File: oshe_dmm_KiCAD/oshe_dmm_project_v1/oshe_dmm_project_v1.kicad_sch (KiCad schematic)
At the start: 65 parts, among them J1 FTDI Basic, J2 USB_C_Receptacle_PowerOnly_6P, J3 ON/OFF, J4 Conn_01x16, SW1 SW_Push, SW2 SW_Rotary_1x4_MP, U1 ATmega328P-A, U2 INA219BxD, U3 BQ24075RGT, U4 LM317_SOT-223, U5 ADS1115IDGS, Y1 16MHz

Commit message: made some more changes!
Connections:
- net GND: now also RV2.3; no longer RV2.2
- net at J4.3 (Pin_3): now also RV2.2; no longer RV2.3
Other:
- moved on the sheet: RV2
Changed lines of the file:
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@@
 	(wire
 		(pts
+			(xy 166.37 45.72) (xy 172.72 45.72)
+		)
+		(stroke
+			(width 0)
+			(type default)
+		)
+	)
+	(wire
+		(pts
 			(xy 332.74 41.91) (xy 345.44 41.91)
 		)
@@
 	(wire
 		(pts
-			(xy 152.4 73.66) (xy 200.66 73.66)
+			(xy 152.4 72.39) (xy 200.66 72.39)
+		)
+		(stroke
+			(width 0)
+			(type default)
+		)
+	)
+	(wire
+		(pts
+			(xy 152.4 49.53) (xy 162.56 49.53)
 		)
 		(stroke
@@
 	(wire
 		(pts
-			(xy 205.74 78.74) (xy 205.74 30.48)
+			(xy 205.74 77.47) (xy 205.74 30.48)
 		)
 		(stroke
@@
 	(wire
 		(pts
-			(xy 152.4 44.45) (xy 158.75 44.45)
-		)
-		(stroke
-			(width 0)
-			(type default)
-		)
-	)
-	(wire
-		(pts
 			(xy 243.84 111.76) (xy 254 111.76)
 		)
@@
 	(wire
 		(pts
-			(xy 193.04 66.04) (xy 193.04 30.48)
+			(xy 193.04 64.77) (xy 193.04 30.48)
 		)
 		(stroke
@@
 	(wire
 		(pts
-			(xy 152.4 60.96) (xy 180.34 60.96)
+			(xy 152.4 59.69) (xy 180.34 59.69)
 		)
 		(stroke
@@
 	(wire
 		(pts
-			(xy 175.26 55.88) (xy 175.26 30.48)
+			(xy 175.26 54.61) (xy 175.26 30.48)
 		)
 		(stroke
@@
 	(wire
 		(pts
-			(xy 152.4 71.12) (xy 198.12 71.12)
+			(xy 152.4 69.85) (xy 198.12 69.85)
 		)
 		(stroke
@@
 	(wire
 		(pts
-			(xy 152.4 58.42) (xy 177.8 58.42)
+			(xy 152.4 57.15) (xy 177.8 57.15)
 		)
 		(stroke
@@
 	(wire
 		(pts
-			(xy 152.4 49.53) (xy 162.56 49.53)
-		)
-		(stroke
-			(width 0)
-			(type default)
-		)
-	)
-	(wire
-		(pts
 			(xy 233.68 58.42) (xy 233.68 60.96)
 		)
@@
 	(wire
 		(pts
-			(xy 195.58 68.58) (xy 195.58 30.48)
+			(xy 195.58 67.31) (xy 195.58 30.48)
 		)
 		(stroke
@@
 	(wire
 		(pts
-			(xy 180.34 60.96) (xy 180.34 30.48)
+			(xy 180.34 59.69) (xy 180.34 30.48)
 		)
 		(stroke
@@
 	(wire
 		(pts
-			(xy 152.4 66.04) (xy 193.04 66.04)
+			(xy 152.4 64.77) (xy 193.04 64.77)
 		)
 		(stroke
@@
 	(wire
 		(pts
+			(xy 172.72 45.72) (xy 172.72 30.48)
+		)
+		(stroke
+			(width 0)
+			(type default)
+		)
+	)
+	(wire
+		(pts
 			(xy 66.04 142.24) (xy 66.04 146.05)
 		)
@@
 	(wire
 		(pts
-			(xy 152.4 55.88) (xy 175.26 55.88)
+			(xy 152.4 54.61) (xy 175.26 54.61)
 		)
 		(stroke
@@
 	(wire
 		(pts
+			(xy 152.4 41.91) (xy 162.56 41.91)
+		)
+		(stroke
+			(width 0)
+			(type default)
+		)
+	)
+	(wire
+		(pts
 			(xy 76.2 161.29) (xy 80.01 161.29)
 		)
@@
 	(wire
 		(pts
-			(xy 152.4 78.74) (xy 205.74 78.74)
+			(xy 152.4 77.47) (xy 205.74 77.47)
 		)
 		(stroke
@@
 	(wire
 		(pts
-			(xy 172.72 44.45) (xy 172.72 30.48)
-		)
-		(stroke
-			(width 0)
-			(type default)
-		)
-	)
-	(wire
-		(pts
 			(xy 261.62 33.02) (xy 285.75 33.02)
 		)
@@
 	(wire
 		(pts
-			(xy 203.2 76.2) (xy 152.4 76.2)
+			(xy 203.2 74.93) (xy 152.4 74.93)
 		)
 		(stroke
@@
 	(wire
 		(pts
-			(xy 152.4 68.58) (xy 195.58 68.58)
+			(xy 152.4 67.31) (xy 195.58 67.31)
 		)
 		(stroke
@@
 	(wire
 		(pts
-			(xy 200.66 73.66) (xy 200.66 30.48)
+			(xy 200.66 72.39) (xy 200.66 30.48)
 		)
 		(stroke
@@
 	(wire
 		(pts
-			(xy 166.37 44.45) (xy 172.72 44.45)
-		)
-		(stroke
-			(width 0)
-			(type default)
-		)
-	)
-	(wire
-		(pts
 			(xy 332.74 49.53) (xy 336.55 49.53)
 		)
@@
 	(wire
 		(pts
-			(xy 177.8 58.42) (xy 177.8 30.48)
+			(xy 177.8 57.15) (xy 177.8 30.48)
 		)
 		(stroke
@@
 	(wire
 		(pts
-			(xy 198.12 71.12) (xy 198.12 30.48)
+			(xy 198.12 69.85) (xy 198.12 30.48)
 		)
 		(stroke
@@
 	(wire
 		(pts
-			(xy 203.2 30.48) (xy 203.2 76.2)
+			(xy 203.2 30.48) (xy 203.2 74.93)
 		)
 		(stroke
@@
 	(wire
 		(pts
-			(xy 162.56 49.53) (xy 162.56 48.26)
-		)
-		(stroke
-			(width 0)
-			(type default)
-		)
-	)
-	(wire
-		(pts
 			(xy 228.6 157.48) (xy 198.12 157.48)
 		)
@@
 	(global_label "GND"
 		(shape input)
-		(at 152.4 78.74 180)
+		(at 152.4 77.47 180)
 		(fields_autoplaced yes)
 		(effects
@@
 		)
 		(property "Intersheetrefs" "${INTERSHEET_REFS}"
-			(at 145.5443 78.74 0)
+			(at 145.5443 77.47 0)
 			(effects
 				(font
@@
 	(global_label "D5"
 		(shape input)
-		(at 152.4 66.04 180)
+		(at 152.4 64.77 180)
 		(fields_autoplaced yes)
 		(effects
@@
 		)
 		(property "Intersheetrefs" "${INTERSHEET_REFS}"
-			(at 146.9353 66.04 0)
+			(at 146.9353 64.77 0)
 			(effects
 				(font
@@
 	(global_label "GND"
 		(shape input)
-		(at 152.4 58.42 180)
+		(at 152.4 57.15 180)
 		(fields_autoplaced yes)
 		(effects
@@
 		)
 		(property "Intersheetrefs" "${INTERSHEET_REFS}"
-			(at 145.5443 58.42 0)
+			(at 145.5443 57.15 0)
 			(effects
 				(font
@@
 	(global_label "+5V"
 		(shape input)
-		(at 152.4 76.2 180)
+		(at 152.4 74.93 180)
 		(fields_autoplaced yes)
 		(effects
@@
 		)
 		(property "Intersheetrefs" "${INTERSHEET_REFS}"
-			(at 145.5443 76.2 0)
+			(at 145.5443 74.93 0)
 			(effects
 				(font
@@
 	(global_label "MISO{slash}D12"
 		(shape input)
-		(at 152.4 60.96 180)
+		(at 152.4 59.69 180)
 		(fields_autoplaced yes)
 		(effects
@@
 		)
 		(property "Intersheetrefs" "${INTERSHEET_REFS}"
-			(at 139.7991 60.96 0)
+			(at 139.7991 59.69 0)
 			(effects
 				(font
@@
 	(global_label "D4"
 		(shape input)
-		(at 152.4 68.58 180)
+		(at 152.4 67.31 180)
 		(fields_autoplaced yes)
 		(effects
@@
 		)
 		(property "Intersheetrefs" "${INTERSHEET_REFS}"
-			(at 146.9353 68.58 0)
+			(at 146.9353 67.31 0)
 			(effects
 				(font
@@
 	(global_label "D3"
 		(shape input)
-		(at 152.4 71.12 180)
+		(at 152.4 69.85 180)
 		(fields_autoplaced yes)
 		(effects
@@
 		)
 		(property "Intersheetrefs" "${INTERSHEET_REFS}"
-			(at 146.9353 71.12 0)
+			(at 146.9353 69.85 0)
 			(effects
 				(font
@@
 	(global_label "D2"
 		(shape input)
-		(at 152.4 73.66 180)
+		(at 152.4 72.39 180)
 		(fields_autoplaced yes)
 		(effects
@@
 		)
 		(property "Intersheetrefs" "${INTERSHEET_REFS}"
-			(at 146.9353 73.66 0)
+			(at 146.9353 72.39 0)
 			(effects
 				(font
@@
 	(global_label "+5V"
 		(shape input)
-		(at 152.4 44.45 180)
+		(at 152.4 41.91 180)
 		(fields_autoplaced yes)
 		(effects
@@
 		)
 		(property "Intersheetrefs" "${INTERSHEET_REFS}"
-			(at 145.5443 44.45 0)
+			(at 145.5443 41.91 0)
 			(effects
 				(font
@@
 	(global_label "MOSI{slash}D11"
 		(shape input)
-		(at 152.4 55.88 180)
+		(at 152.4 54.61 180)
 		(fields_autoplaced yes)
 		(effects
@@
 		)
 		(property "Intersheetrefs" "${INTERSHEET_REFS}"
-			(at 139.7991 55.88 0)
+			(at 139.7991 54.61 0)
 			(effects
 				(font
@@
 	(symbol
 		(lib_id "Device:R_Potentiometer_US")
-		(at 162.56 44.45 90)
-		(mirror x)
+		(at 162.56 45.72 0)
 		(unit 1)
 		(exclude_from_sim no)
@@
 		(dnp no)
 		(property "Reference" "RV2"
-			(at 162.56 38.862 90)
+			(at 158.115 46.863 0)
 			(effects
 				(font
@@
 		)
 		(property "Value" "10k"
-			(at 162.56 41.402 90)
+			(at 158.115 44.323 0)
 			(effects
 				(font
@@
 		)
 		(property "Footprint" "Potentiometer_SMD:Potentiometer_ACP_CA6-VSMD_Vertical"
-			(at 162.56 44.45 0)
+			(at 162.56 45.72 0)
 			(effects
 				(font
@@
 		)
 		(property "Datasheet" "~"
-			(at 162.56 44.45 0)
+			(at 162.56 45.72 0)
 			(effects
 				(font
@@
 		)
 		(property "Description" "Potentiometer, US symbol"
-			(at 162.56 44.45 0)
+			(at 162.56 45.72 0)
 			(effects
 				(font

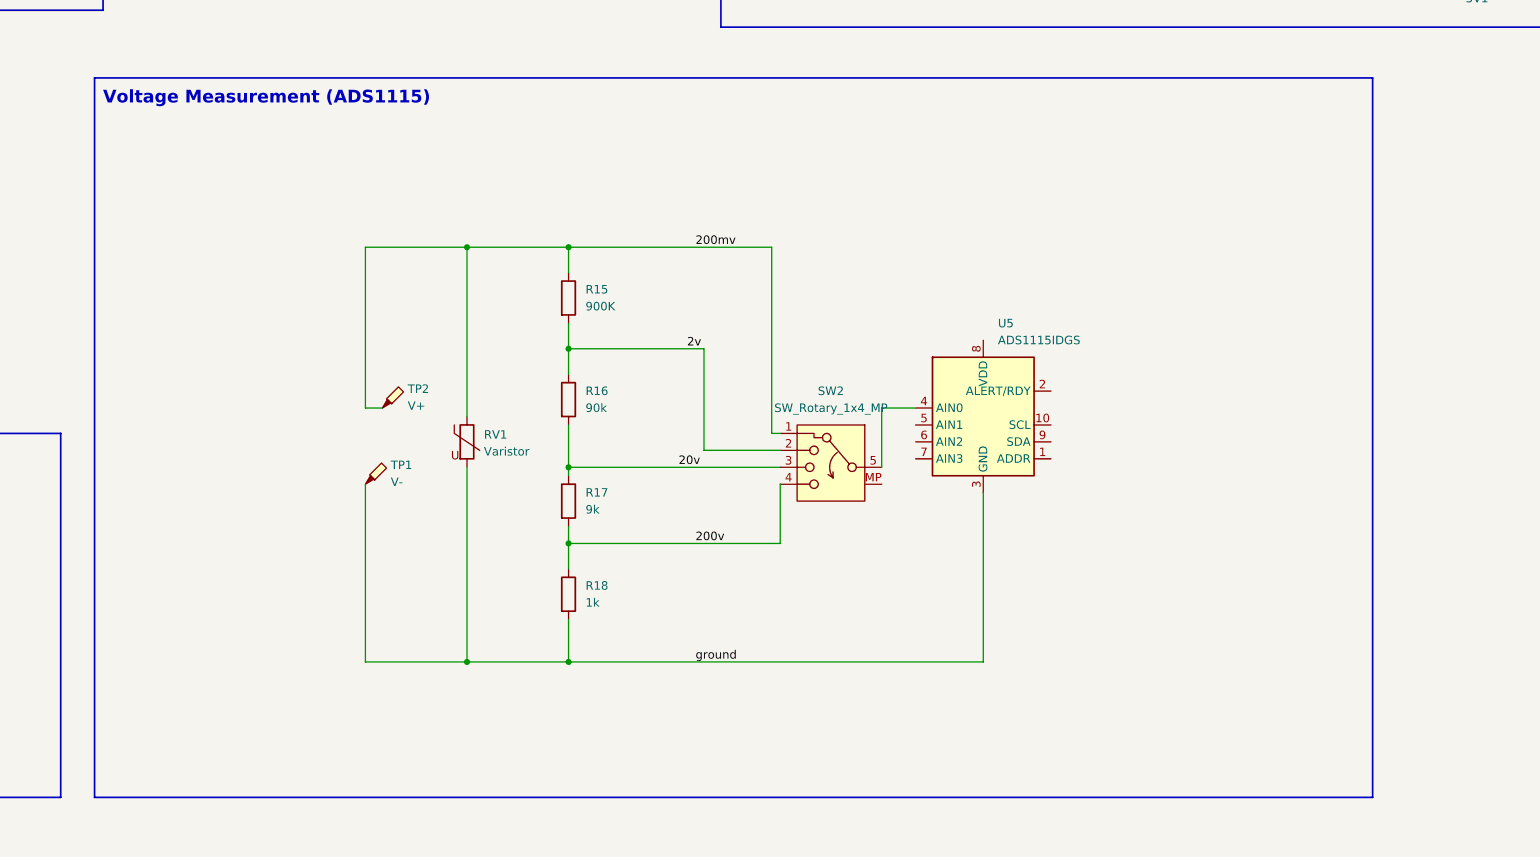
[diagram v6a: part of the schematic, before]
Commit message: Update oshe_dmm_project_v1.kicad_sch
Updated voltage schematic.
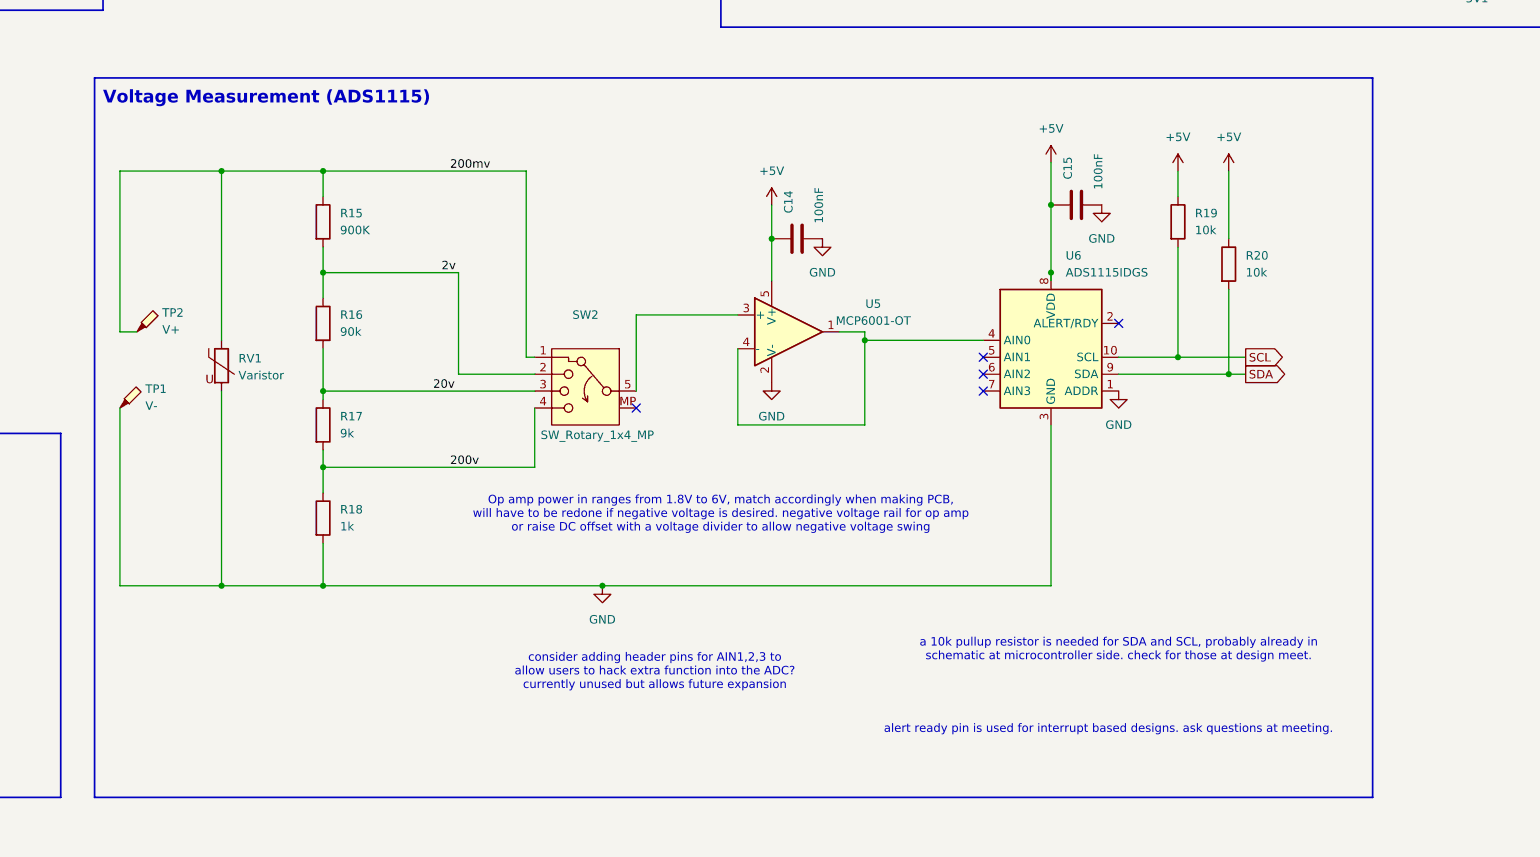
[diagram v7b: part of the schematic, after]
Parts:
- removed U5: ADS1115IDGS, Package_SO:TSSOP-10_3x3mm_P0.5mm, symbol Analog_ADC:ADS1115IDGS
- added C14, C15: 100nF, symbol Device:C
- added R19, R20: 10k, symbol Device:R
- added U5: MCP6001-OT, Package_TO_SOT_SMD:SOT-23-5, symbol Amplifier_Operational:MCP6001-OT
- added U6: ADS1115IDGS, Package_SO:TSSOP-10_3x3mm_P0.5mm, symbol Analog_ADC:ADS1115IDGS
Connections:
- net ground is gone; now on net GND: R18.2, RV1.2, TP1.1
- net +5V: now also C14.1, C15.1, R19.1, R20.1, U5.5 (V+), U6.8 (VDD)
- net GND: now also C14.2, C15.2, U5.2 (V-), U6.1 (ADDR), U6.3 (GND)
- net SCL: now also R19.2, U6.10 (SCL)
- net SDA: now also R20.2, U6.9 (SDA)
- net at SW2.5: now also U5.3 (+)
- new net: U5.1, U5.4 (-), U6.4 (AIN0)
- no-connect marks 7 -> 12
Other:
- note added: "Op amp power in ranges from 1.8V to 6V, match accordingly when making PCB, will have to be redone if negative voltage is desired. negative voltage rail for op amp or raise DC offset with a voltage divider to allow negative voltage swing"
- note added: "a 10k pullup resistor is needed for SDA and SCL, probably already in schematic at microcontroller side. check for those at design meet."
- note added: "alert ready pin is used for interrupt based designs. ask questions at meeting."
- note added: "consider adding header pins for AIN1,2,3 to allow users to hack extra function into the ADC? currently unused but allows future expansion"

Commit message: Made some changes!
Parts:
- removed J4: Conn_01x16, Connector_PinSocket_2.54mm:PinSocket_1x16_P2.54mm_Vertical, symbol Connector_Generic:Conn_01x16
- added DS1: WC1602A, Display:WC1602A, symbol Display_Character:WC1602A
- J1: now not fitted
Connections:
- net +5V: now also DS1.15 (LED(+)), DS1.2 (VDD)
- net D2: now also DS1.14 (D7)
- net D3: now also DS1.13 (D6)
- net D4: now also DS1.12 (D5)
- net D5: now also DS1.11 (D4)
- net GND: now also DS1.1 (VSS), DS1.16 (LED(-)), DS1.5 (R/W)
- net MISO/D12: now also DS1.6 (E)
- net MOSI/D11: now also DS1.4 (RS)
- net at RV2.2: now also DS1.3 (VO)
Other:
- moved on the sheet: C14, C15, R15, R16, R17, R18, R19, R20, R9, RV1, SW2, TP1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
